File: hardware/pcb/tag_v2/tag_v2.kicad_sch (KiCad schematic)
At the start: 12 parts

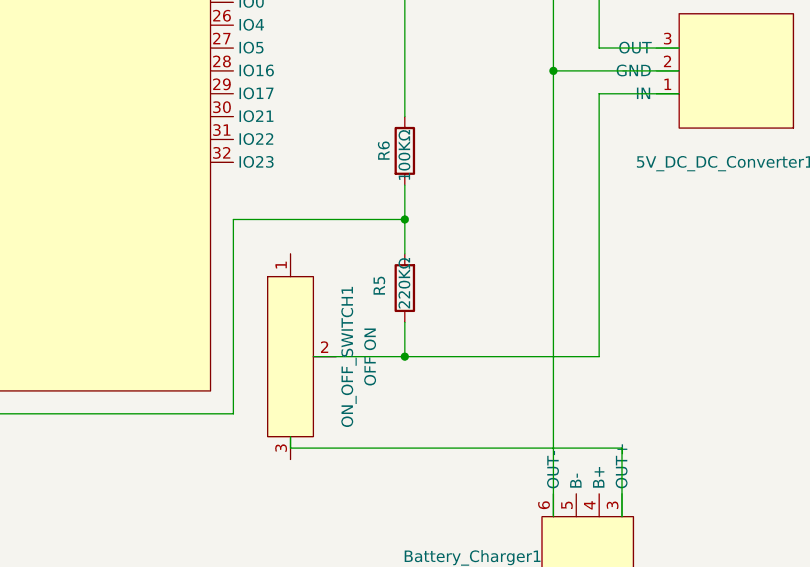
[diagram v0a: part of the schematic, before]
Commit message: *: Update after the first PCB assembly.
- Replaced the 200k ohm resistor with 100k ohm on tag_v2, as GPIO pin 32
  reduces the voltage somehow, updated the battery voltage divider
  accordingly in tag.ino

- Fix an issue of tag LED as the tag will not invoke newDevice() even
  though it's added by the Sensor.

- Updated the DRIVE_MODE_MANUAL to be long steady light instead of
  blincking.

- Fixed a short wiring issue on the sensor.
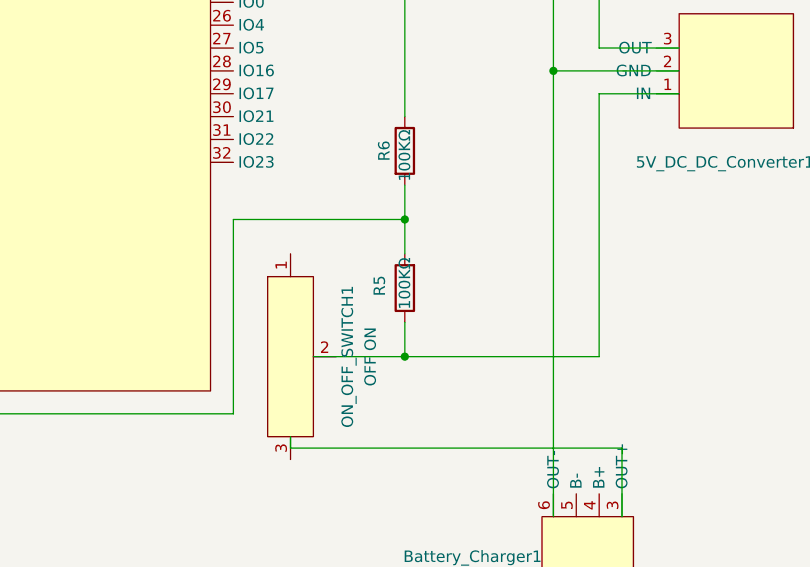
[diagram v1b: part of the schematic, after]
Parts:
- R5: value 220KΩ -> 100KΩ
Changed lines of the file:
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@@
 	(title_block
 		(title "Autocam Tag")
-		(date "2025-03-18")
-		(rev "v0.4")
+		(date "2025-03-26")
+		(rev "v0.5")
 	)
 	(junction
@@
 			)
 		)
-		(property "Value" "220KΩ"
+		(property "Value" "100KΩ"
 			(at 180.34 117.602 90)
 			(effects

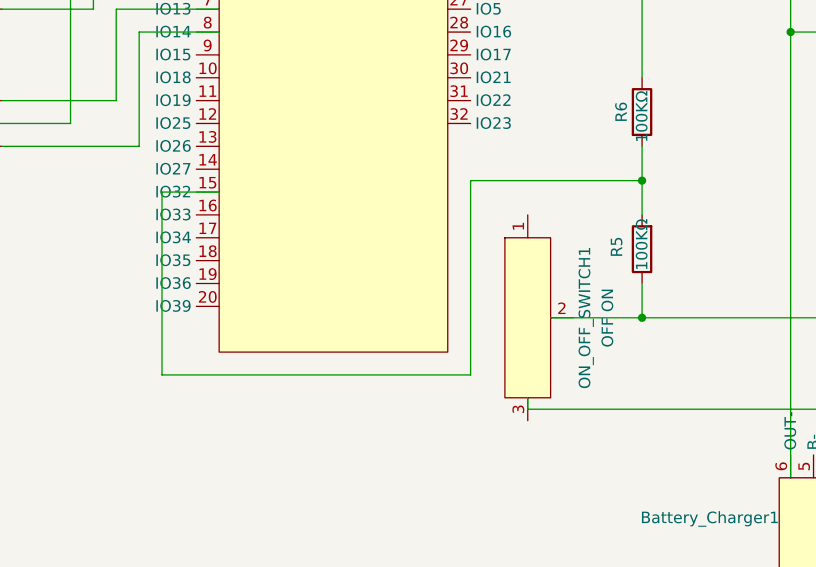
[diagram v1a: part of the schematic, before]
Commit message: remote: Update PCB for remote.
Fix the issue that GPIO 35 does not have internal PULLUP resistor.
So switch the pin with the gimbal thumbstick input Y, instead of the
drive mode button.

Update sensor and tag pcb as well to reflect the changes.
- tag: Use pin 39 for battery measurement and revert the resistor value
  change that's done in the previous commit.
- sensor: Fix a wiring issue.
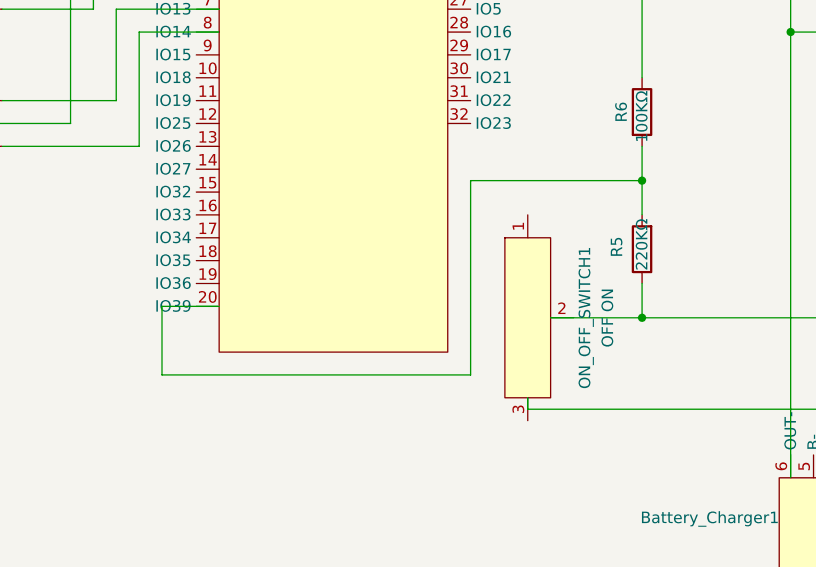
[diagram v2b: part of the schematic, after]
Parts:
- R5: value 100KΩ -> 220KΩ
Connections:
- net at R5.2, R6.2: now also ESP32_UWB1.20 (IO39); no longer ESP32_UWB1.15 (IO32)
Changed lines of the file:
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@@
+	(wire
+		(pts
+			(xy 133.35 124.46) (xy 127 124.46)
+		)
+		(stroke
+			(width 0)
+			(type default)
+		)
+	)
 	(wire
 		(pts
@@
 	(wire
 		(pts
-			(xy 127 111.76) (xy 127 132.08)
-		)
-		(stroke
-			(width 0)
-			(type default)
-		)
-	)
-	(wire
-		(pts
 			(xy 158.75 78.74) (xy 180.34 78.74)
 		)
@@
 	(wire
 		(pts
-			(xy 127 111.76) (xy 133.35 111.76)
-		)
-		(stroke
-			(width 0)
-			(type default)
-		)
-	)
-	(wire
-		(pts
 			(xy 87.63 104.14) (xy 116.84 104.14)
 		)
@@
 		(pts
 			(xy 201.93 96.52) (xy 201.93 125.73)
+		)
+		(stroke
+			(width 0)
+			(type default)
+		)
+	)
+	(wire
+		(pts
+			(xy 127 124.46) (xy 127 132.08)
 		)
 		(stroke
@@
 			)
 		)
-		(property "Value" "100KΩ"
+		(property "Value" "220KΩ"
 			(at 180.34 117.602 90)
 			(effects

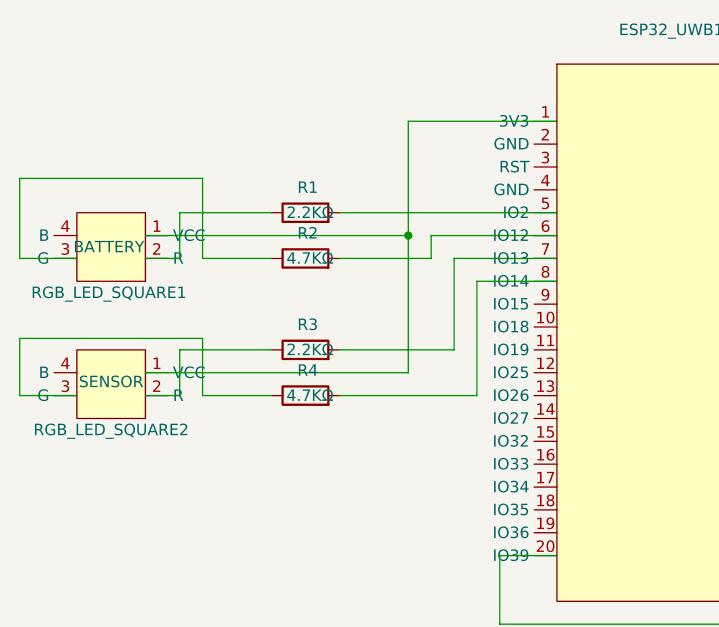
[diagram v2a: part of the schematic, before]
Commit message: sensor,tag: Update PCB wiring to avoid bootstrap pins.
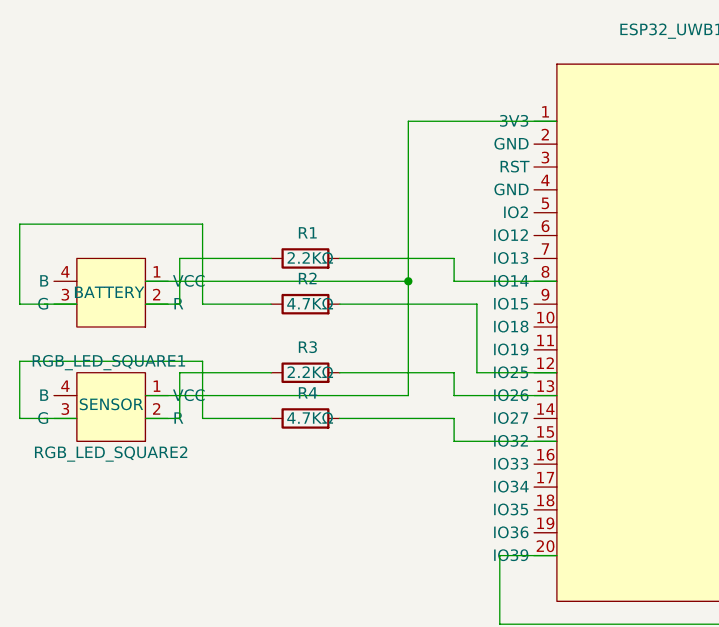
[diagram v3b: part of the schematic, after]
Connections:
- net at R4.2: now also ESP32_UWB1.15 (IO32); no longer ESP32_UWB1.8 (IO14)
- net at R3.2: now also ESP32_UWB1.13 (IO26); no longer ESP32_UWB1.7 (IO13)
- net at ESP32_UWB1.12 (IO25): now also R2.2
- net at ESP32_UWB1.5 (IO2): no longer R1.2
- net at ESP32_UWB1.6 (IO12): no longer R2.2
- new net: ESP32_UWB1.8 (IO14), R1.2
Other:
- moved on the sheet: R1, R2, R3, R4, RGB_LED_SQUARE1, RGB_LED_SQUARE2
